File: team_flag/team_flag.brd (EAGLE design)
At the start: 40.6 x 40.6 mm, 11 parts, among them Q1 MOSFET-LOGIC-NCHANNELSMD, Q2 MOSFET-LOGIC-NCHANNELSMD

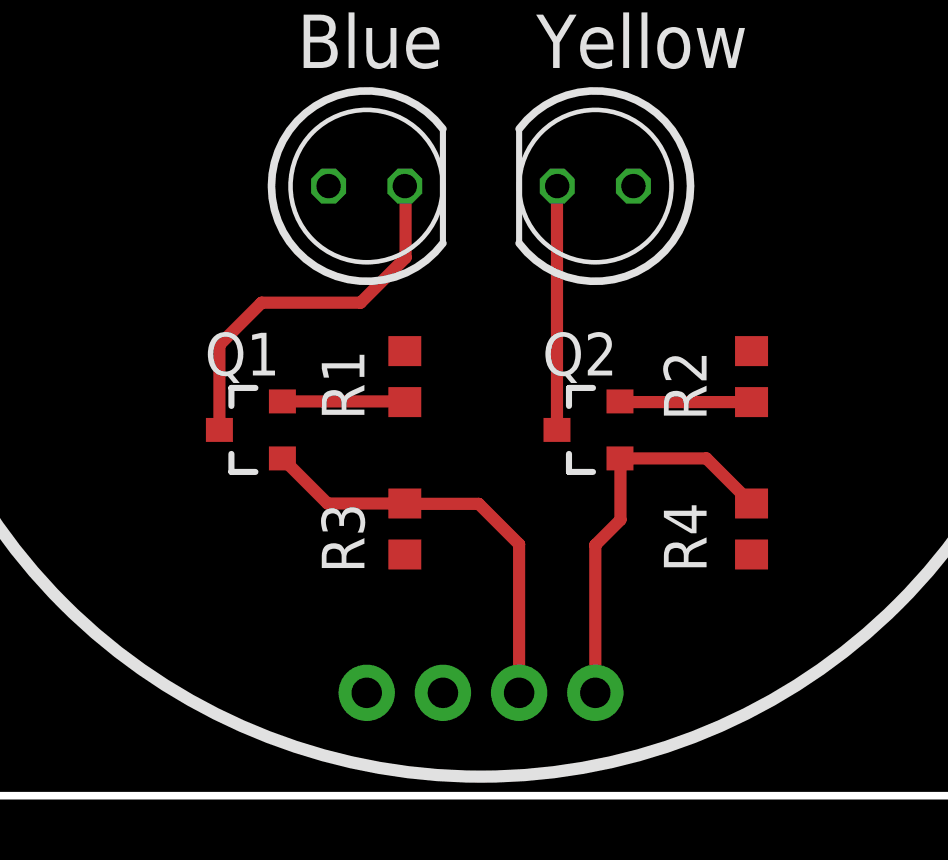
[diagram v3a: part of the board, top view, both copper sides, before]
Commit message: Team Flag Rev C pt 2
-changed resistors from 200 to 330
-moved 330 resistors to the drain-side of the MOSFETs
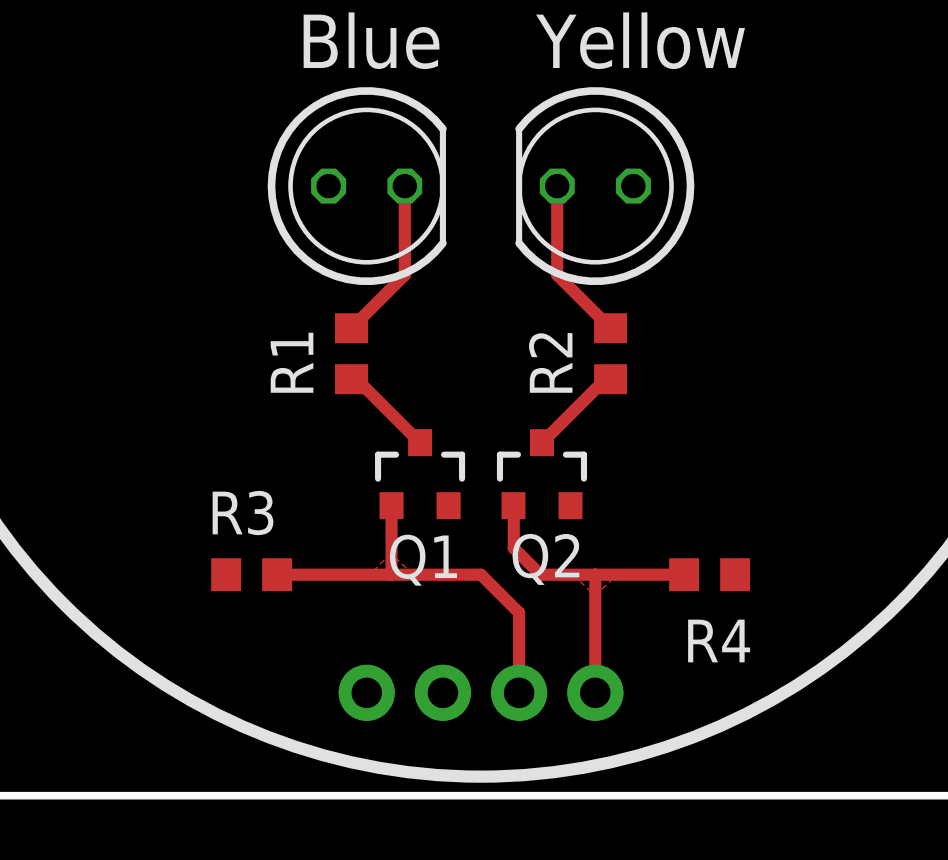
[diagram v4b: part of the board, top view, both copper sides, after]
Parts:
- R1, R2: value 200 -> 330
- moved Q1 5.79 mm to (18.3, 10.7), turned to 0 degrees
- moved R3 5.33 mm to (12.7, 7.37), turned to 0 degrees
- moved R2 4.76 mm to (24.6, 14.7), turned to 90 degrees
- moved Q2 2.21 mm to (22.4, 10.7), turned to 0 degrees
- moved R4 2.07 mm to (27.9, 7.37), turned to 180 degrees
- moved R1 1.93 mm to (16.0, 14.7), turned to 90 degrees
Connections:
- removed net BDRAIN: LED1.K, Q1.3
- removed net YDRAIN: LED2.K, Q2.3
- new net N$2: LED1.K, R1.2
- new net N$3: LED2.K, R2.2
- net BSOURCE: now also Q1.3, R1.1; no longer Q1.2, R1.2
- net GND: now also Q1.2, Q2.2; no longer R1.1, R2.1
- net YSOURCE: now also Q2.3, R2.1; no longer Q2.2, R2.2
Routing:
- net BDRAIN: track 12.6 -> 0.00 mm
- net YDRAIN: track 8.13 -> 0.00 mm
- net N$3: track 0.00 -> 5.47 mm
- net N$2: track 0.00 -> 5.47 mm
- net YELLOW: track 13.2 -> 11.4 mm
- net YSOURCE: track 4.41 -> 3.16 mm
- net BSOURCE: track 4.10 -> 3.16 mm
- added copper zone on layer 1, net BLUE
- added copper zone on layer 1, net YELLOW
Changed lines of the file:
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@@
 <attribute name="VALUE" x="20.9296" y="22.1234" size="1.27" layer="27" ratio="10" rot="R180"/>
 </element>
-<element name="R1" library="rcl" package="R0603" value="200" x="17.78" y="13.97" smashed="yes" rot="R270">
-<attribute name="NAME" x="16.4338" y="12.5222" size="1.4224" layer="25" font="vector" rot="R90"/>
-<attribute name="VALUE" x="20.5232" y="12.4968" size="1.4224" layer="27" font="vector" rot="R90"/>
+<element name="R1" library="rcl" package="R0603" value="330" x="16.002" y="14.732" smashed="yes" rot="R90">
+<attribute name="NAME" x="14.732" y="13.2588" size="1.4224" layer="25" font="vector" rot="R90"/>
+<attribute name="VALUE" x="17.272" y="13.2588" size="1.4224" layer="27" font="vector" rot="R270" align="bottom-right"/>
 </element>
-<element name="R2" library="rcl" package="R0603" value="200" x="29.337" y="13.97" smashed="yes" rot="R270">
-<attribute name="NAME" x="27.8384" y="12.4968" size="1.4224" layer="25" font="vector" rot="R90"/>
-<attribute name="VALUE" x="32.004" y="12.4968" size="1.4224" layer="27" font="vector" rot="R90"/>
+<element name="R2" library="rcl" package="R0603" value="330" x="24.638" y="14.732" smashed="yes" rot="R90">
+<attribute name="NAME" x="23.368" y="13.2588" size="1.4224" layer="25" font="vector" rot="R90"/>
+<attribute name="VALUE" x="25.8826" y="13.2588" size="1.4224" layer="27" font="vector" rot="R270" align="bottom-right"/>
 </element>
 <element name="U$2" library="pie" package="OSHW-LOGO-S" value="" x="20.32" y="31.75" rot="MR0"/>
 <element name="U$1" library="pie" package="PIE-LOGO-SMALL" value="" x="33.655" y="16.51" rot="MR0"/>
-<element name="Q1" library="pie" package="SOT23-3-LOGIC" value="MOSFET-LOGIC-NCHANNELSMD" x="12.7" y="12.192" smashed="yes" rot="R90">
-<attribute name="NAME" x="13.6144" y="15.4305" size="1.4224" layer="25" font="vector" align="top-right"/>
-<attribute name="PIE_DIGIKEY-PN" value="DMN65D8L-7DICT-ND" x="12.7" y="12.192" size="1.778" layer="27" rot="R90" display="off"/>
+<element name="Q1" library="pie" package="SOT23-3-LOGIC" value="MOSFET-LOGIC-NCHANNELSMD" x="18.288" y="10.668" smashed="yes">
+<attribute name="NAME" x="19.685" y="7.2517" size="1.4224" layer="25" font="vector" rot="R180" align="top-left"/>
+<attribute name="PIE_DIGIKEY-PN" value="DMN65D8L-7DICT-ND" x="18.288" y="10.668" size="1.778" layer="27" display="off"/>
 </element>
-<element name="Q2" library="pie" package="SOT23-3-LOGIC" value="MOSFET-LOGIC-NCHANNELSMD" x="23.9522" y="12.192" smashed="yes" rot="R90">
-<attribute name="NAME" x="24.8666" y="15.4305" size="1.4224" layer="25" font="vector" rot="R180"/>
-<attribute name="PIE_DIGIKEY-PN" value="DMN65D8L-7DICT-ND" x="23.9522" y="12.192" size="1.778" layer="27" rot="R90" display="off"/>
+<element name="Q2" library="pie" package="SOT23-3-LOGIC" value="MOSFET-LOGIC-NCHANNELSMD" x="22.352" y="10.668" smashed="yes">
+<attribute name="NAME" x="23.7744" y="7.2771" size="1.4224" layer="25" font="vector" align="bottom-right"/>
+<attribute name="PIE_DIGIKEY-PN" value="DMN65D8L-7DICT-ND" x="22.352" y="10.668" size="1.778" layer="27" display="off"/>
 </element>
-<element name="R3" library="rcl" package="R0603" value="10K" x="17.78" y="8.89" smashed="yes" rot="R90">
-<attribute name="NAME" x="16.4338" y="7.4168" size="1.4224" layer="25" font="vector" rot="R90"/>
-<attribute name="VALUE" x="20.5232" y="7.4168" size="1.4224" layer="27" font="vector" rot="R90"/>
+<element name="R3" library="rcl" package="R0603" value="10K" x="12.6746" y="7.366" smashed="yes">
+<attribute name="NAME" x="11.2014" y="8.7122" size="1.4224" layer="25" font="vector"/>
+<attribute name="VALUE" x="11.2014" y="4.6228" size="1.4224" layer="27" font="vector"/>
 </element>
-<element name="R4" library="rcl" package="R0603" value="10K" x="29.337" y="8.89" smashed="yes" rot="R90">
-<attribute name="NAME" x="27.8384" y="7.4422" size="1.4224" layer="25" font="vector" rot="R90"/>
-<attribute name="VALUE" x="32.1564" y="7.4168" size="1.4224" layer="27" font="vector" rot="R90"/>
+<element name="R4" library="rcl" package="R0603" value="10K" x="27.94" y="7.366" smashed="yes" rot="R180">
+<attribute name="NAME" x="29.3878" y="5.8674" size="1.4224" layer="25" font="vector" rot="R180"/>
+<attribute name="VALUE" x="29.4132" y="10.1854" size="1.4224" layer="27" font="vector" rot="R180"/>
 </element>
 <element name="JP1" library="pie" package="1X04-MTA" value="" x="20.32" y="3.429" smashed="yes" rot="MR180">
@@
 <contactref element="R4" pad="2"/>
 <contactref element="JP1" pad="4"/>
-<wire x1="24.13" y1="3.429" x2="24.13" y2="8.3566" width="0.4064" layer="1"/>
-<wire x1="24.13" y1="8.3566" x2="24.9682" y2="9.1948" width="0.4064" layer="1"/>
-<wire x1="24.9682" y1="9.1948" x2="24.9682" y2="11.226" width="0.4064" layer="1"/>
-<wire x1="24.9682" y1="11.226" x2="24.9522" y2="11.242" width="0.4064" layer="1"/>
-<wire x1="29.337" y1="9.74" x2="27.835" y2="11.242" width="0.4064" layer="1"/>
-<wire x1="27.835" y1="11.242" x2="24.9522" y2="11.242" width="0.4064" layer="1"/>
+<wire x1="27.09" y1="7.366" x2="24.13" y2="7.366" width="0.4064" layer="1"/>
+<wire x1="24.13" y1="7.366" x2="22.3012" y2="7.366" width="0.4064" layer="1"/>
+<wire x1="22.3012" y1="7.366" x2="21.4122" y2="8.255" width="0.4064" layer="1"/>
+<wire x1="21.4122" y1="8.255" x2="21.4122" y2="9.6578" width="0.4064" layer="1"/>
+<wire x1="21.4122" y1="9.6578" x2="21.402" y2="9.668" width="0.4064" layer="1"/>
+<wire x1="24.13" y1="3.429" x2="24.13" y2="7.366" width="0.4064" layer="1"/>
+<polygon width="0.4064" layer="1" spacing="0.6096">
+<vertex x="23.3934" y="7.366"/>
+<vertex x="24.13" y="6.6548"/>
+<vertex x="24.8412" y="7.366"/>
+</polygon>
 </signal>
 <signal name="VCC">
@@
 </signal>
 <signal name="GND">
-<contactref element="R1" pad="1"/>
-<contactref element="R2" pad="1"/>
 <polygon width="0.4064" layer="1" rank="2">
 <vertex x="0" y="0"/>
@@
 <contactref element="R4" pad="1"/>
 <contactref element="JP1" pad="1"/>
+<contactref element="Q1" pad="2"/>
+<contactref element="Q2" pad="2"/>
 </signal>
 <signal name="BLUE">
@@
 <contactref element="R3" pad="2"/>
 <contactref element="JP1" pad="3"/>
-<wire x1="21.59" y1="3.429" x2="21.59" y2="8.382" width="0.4064" layer="1"/>
-<wire x1="21.59" y1="8.382" x2="20.2438" y2="9.7282" width="0.4064" layer="1"/>
-<wire x1="20.2438" y1="9.7282" x2="17.7918" y2="9.7282" width="0.4064" layer="1"/>
-<wire x1="17.7918" y1="9.7282" x2="17.78" y2="9.74" width="0.4064" layer="1"/>
-<wire x1="17.78" y1="9.74" x2="15.202" y2="9.74" width="0.4064" layer="1"/>
-<wire x1="15.202" y1="9.74" x2="13.7" y2="11.242" width="0.4064" layer="1"/>
-</signal>
-<signal name="BDRAIN">
-<contactref element="LED1" pad="K"/>
-<contactref element="Q1" pad="3"/>
-<wire x1="11.6" y1="12.192" x2="11.6" y2="15.029" width="0.4064" layer="1"/>
-<wire x1="11.6" y1="15.029" x2="13.0048" y2="16.4338" width="0.4064" layer="1"/>
-<wire x1="13.0048" y1="16.4338" x2="16.3068" y2="16.4338" width="0.4064" layer="1"/>
-<wire x1="16.3068" y1="16.4338" x2="17.8054" y2="17.9324" width="0.4064" layer="1"/>
-<wire x1="17.8054" y1="17.9324" x2="17.8054" y2="20.2946" width="0.4064" layer="1"/>
-<wire x1="17.8054" y1="20.2946" x2="17.78" y2="20.32" width="0.4064" layer="1"/>
+<wire x1="21.59" y1="3.429" x2="21.59" y2="6.096" width="0.4064" layer="1"/>
+<wire x1="21.59" y1="6.096" x2="20.32" y2="7.366" width="0.4064" layer="1"/>
+<wire x1="20.32" y1="7.366" x2="17.2974" y2="7.366" width="0.4064" layer="1"/>
+<wire x1="17.2974" y1="7.366" x2="13.5246" y2="7.366" width="0.4064" layer="1"/>
+<wire x1="17.338" y1="9.668" x2="17.338" y2="7.4066" width="0.4064" layer="1"/>
+<wire x1="17.338" y1="7.4066" x2="17.2974" y2="7.366" width="0.4064" layer="1"/>
+<polygon width="0.4064" layer="1" spacing="0.6096">
+<vertex x="18.0594" y="7.366"/>
+<vertex x="17.3228" y="8.0772"/>
+<vertex x="16.6116" y="7.366"/>
+</polygon>
 </signal>
 <signal name="BSOURCE">
-<contactref element="Q1" pad="2"/>
+<contactref element="Q1" pad="3"/>
+<contactref element="R1" pad="1"/>
+<wire x1="16.002" y1="13.882" x2="16.174" y2="13.882" width="0.4064" layer="1"/>
+<wire x1="16.174" y1="13.882" x2="18.288" y2="11.768" width="0.4064" layer="1"/>
+</signal>
+<signal name="N$2">
 <contactref element="R1" pad="2"/>
-<wire x1="13.7" y1="13.142" x2="17.78" y2="13.142" width="0.4064" layer="1"/>
-<wire x1="17.78" y1="13.142" x2="17.78" y2="13.12" width="0.4064" layer="1"/>
+<contactref element="LED1" pad="K"/>
+<wire x1="16.002" y1="15.582" x2="17.78" y2="17.36" width="0.4064" layer="1"/>
+<wire x1="17.78" y1="17.36" x2="17.78" y2="20.32" width="0.4064" layer="1"/>
 </signal>
-<signal name="YDRAIN">
+<signal name="N$3">
 <contactref element="LED2" pad="K"/>
-<contactref element="Q2" pad="3"/>
-<wire x1="22.8522" y1="12.192" x2="22.8522" y2="20.3122" width="0.4064" layer="1"/>
-<wire x1="22.8522" y1="20.3122" x2="22.86" y2="20.32" width="0.4064" layer="1"/>
+<contactref element="R2" pad="2"/>
+<wire x1="24.638" y1="15.582" x2="22.86" y2="17.36" width="0.4064" layer="1"/>
+<wire x1="22.86" y1="17.36" x2="22.86" y2="20.32" width="0.4064" layer="1"/>
 </signal>
 <signal name="YSOURCE">
-<contactref element="Q2" pad="2"/>
-<contactref element="R2" pad="2"/>
-<wire x1="29.337" y1="13.12" x2="24.9522" y2="13.12" width="0.4064" layer="1"/>
-<wire x1="24.9522" y1="13.12" x2="24.9522" y2="13.142" width="0.4064" layer="1"/>
+<contactref element="R2" pad="1"/>
+<contactref element="Q2" pad="3"/>
+<wire x1="24.638" y1="13.882" x2="24.466" y2="13.882" width="0.4064" layer="1"/>
+<wire x1="24.466" y1="13.882" x2="22.352" y2="11.768" width="0.4064" layer="1"/>
 </signal>
 </signals>

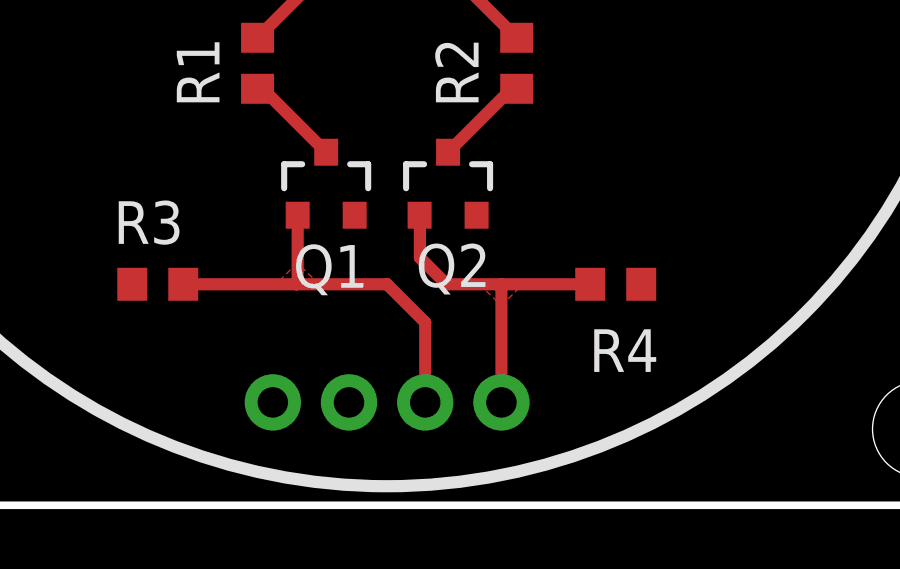
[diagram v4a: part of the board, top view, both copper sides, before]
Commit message: Team Flag Rev C pt 3
-reoriented MTA connector footprint
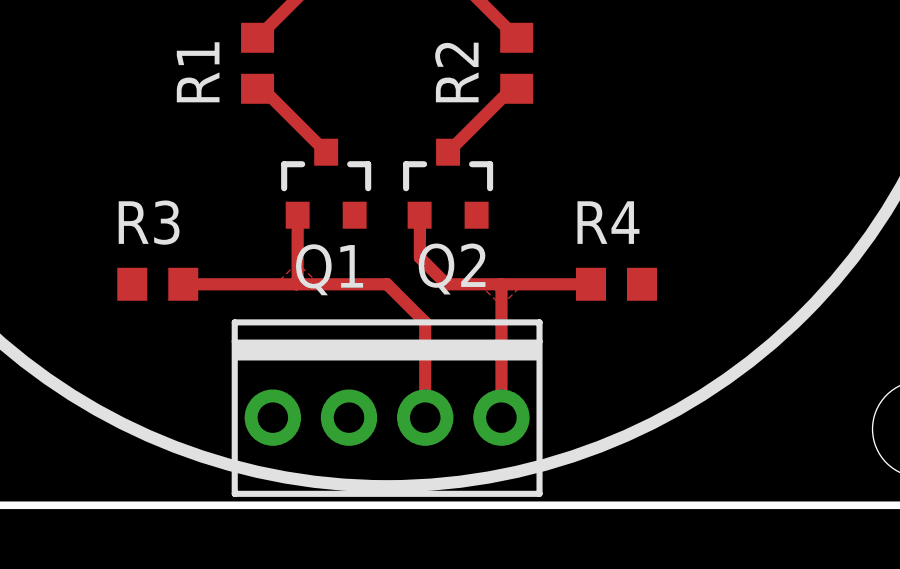
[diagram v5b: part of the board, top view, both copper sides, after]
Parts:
- moved JP1 0.51 mm to (20.3, 2.92), flipped to the top, turned to 0 degrees
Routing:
- net YELLOW: track 11.4 -> 11.9 mm
- net BLUE: track 13.6 -> 14.1 mm
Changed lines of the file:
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@@
 <attribute name="VALUE" x="11.2014" y="4.6228" size="1.4224" layer="27" font="vector"/>
 </element>
-<element name="R4" library="rcl" package="R0603" value="10K" x="27.94" y="7.366" smashed="yes" rot="R180">
-<attribute name="NAME" x="29.3878" y="5.8674" size="1.4224" layer="25" font="vector" rot="R180"/>
-<attribute name="VALUE" x="29.4132" y="10.1854" size="1.4224" layer="27" font="vector" rot="R180"/>
+<element name="R4" library="rcl" package="R0603" value="10K" x="27.9654" y="7.366" smashed="yes" rot="R180">
+<attribute name="NAME" x="26.4922" y="8.7122" size="1.4224" layer="25" font="vector" rot="R180" align="top-right"/>
+<attribute name="VALUE" x="26.4922" y="4.6228" size="1.4224" layer="27" font="vector" rot="R180" align="top-right"/>
 </element>
-<element name="JP1" library="pie" package="1X04-MTA" value="" x="20.32" y="3.429" smashed="yes" rot="MR180">
-<attribute name="PARTNUMBER" value="A1922-ND" x="20.32" y="3.429" size="1.778" layer="28" rot="MR180" display="off"/>
-<attribute name="VALUE" x="15.875" y="7.874" size="1.27" layer="28" font="vector" rot="MR180"/>
+<element name="JP1" library="pie" package="1X04-MTA" value="" x="20.32" y="2.921" smashed="yes">
+<attribute name="PARTNUMBER" value="A1922-ND" x="20.32" y="2.921" size="1.778" layer="27" display="off"/>
+<attribute name="VALUE" x="15.875" y="-1.524" size="1.27" layer="27" font="vector"/>
 </element>
 </elements>
@@
 <contactref element="R4" pad="2"/>
 <contactref element="JP1" pad="4"/>
-<wire x1="27.09" y1="7.366" x2="24.13" y2="7.366" width="0.4064" layer="1"/>
-<wire x1="24.13" y1="7.366" x2="22.3012" y2="7.366" width="0.4064" layer="1"/>
+<wire x1="27.1154" y1="7.366" x2="24.1046" y2="7.366" width="0.4064" layer="1"/>
+<wire x1="24.1046" y1="7.366" x2="22.3012" y2="7.366" width="0.4064" layer="1"/>
 <wire x1="22.3012" y1="7.366" x2="21.4122" y2="8.255" width="0.4064" layer="1"/>
 <wire x1="21.4122" y1="8.255" x2="21.4122" y2="9.6578" width="0.4064" layer="1"/>
 <wire x1="21.4122" y1="9.6578" x2="21.402" y2="9.668" width="0.4064" layer="1"/>
-<wire x1="24.13" y1="3.429" x2="24.13" y2="7.366" width="0.4064" layer="1"/>
 <polygon width="0.4064" layer="1" spacing="0.6096">
 <vertex x="23.3934" y="7.366"/>
@@
 <vertex x="24.8412" y="7.366"/>
 </polygon>
+<wire x1="24.13" y1="2.921" x2="24.13" y2="7.3406" width="0.4064" layer="1"/>
+<wire x1="24.13" y1="7.3406" x2="24.1046" y2="7.366" width="0.4064" layer="1"/>
 </signal>
 <signal name="VCC">
@@
 <contactref element="R3" pad="2"/>
 <contactref element="JP1" pad="3"/>
-<wire x1="21.59" y1="3.429" x2="21.59" y2="6.096" width="0.4064" layer="1"/>
 <wire x1="21.59" y1="6.096" x2="20.32" y2="7.366" width="0.4064" layer="1"/>
 <wire x1="20.32" y1="7.366" x2="17.2974" y2="7.366" width="0.4064" layer="1"/>
@@
 <vertex x="16.6116" y="7.366"/>
 </polygon>
+<wire x1="21.59" y1="2.921" x2="21.59" y2="6.096" width="0.4064" layer="1"/>
 </signal>
 <signal name="BSOURCE">

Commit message: Team Flag Rev C pt 4
-reoriented MTA footprint again
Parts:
- flipped JP1 to the bottom
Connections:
- net BLUE: now also JP1.2; no longer JP1.3
- net GND: now also JP1.4; no longer JP1.1
- net VCC: now also JP1.3; no longer JP1.2
- net YELLOW: now also JP1.1; no longer JP1.4
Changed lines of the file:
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@@
 <attribute name="VALUE" x="26.4922" y="4.6228" size="1.4224" layer="27" font="vector" rot="R180" align="top-right"/>
 </element>
-<element name="JP1" library="pie" package="1X04-MTA" value="" x="20.32" y="2.921" smashed="yes">
-<attribute name="PARTNUMBER" value="A1922-ND" x="20.32" y="2.921" size="1.778" layer="27" display="off"/>
-<attribute name="VALUE" x="15.875" y="-1.524" size="1.27" layer="27" font="vector"/>
+<element name="JP1" library="pie" package="1X04-MTA" value="" x="20.32" y="2.921" smashed="yes" rot="MR0">
+<attribute name="PARTNUMBER" value="A1922-ND" x="20.32" y="2.921" size="1.778" layer="28" rot="MR0" display="off"/>
+<attribute name="VALUE" x="24.765" y="-1.524" size="1.27" layer="28" font="vector" rot="MR0"/>
 </element>
 </elements>
@@
 <contactref element="Q2" pad="1"/>
 <contactref element="R4" pad="2"/>
-<contactref element="JP1" pad="4"/>
 <wire x1="27.1154" y1="7.366" x2="24.1046" y2="7.366" width="0.4064" layer="1"/>
 <wire x1="24.1046" y1="7.366" x2="22.3012" y2="7.366" width="0.4064" layer="1"/>
@@
 <vertex x="24.8412" y="7.366"/>
 </polygon>
+<wire x1="24.13" y1="7.3406" x2="24.1046" y2="7.366" width="0.4064" layer="1"/>
+<contactref element="JP1" pad="1"/>
 <wire x1="24.13" y1="2.921" x2="24.13" y2="7.3406" width="0.4064" layer="1"/>
-<wire x1="24.13" y1="7.3406" x2="24.1046" y2="7.366" width="0.4064" layer="1"/>
 </signal>
 <signal name="VCC">
@@
 <contactref element="LED1" pad="A"/>
 <contactref element="LED2" pad="A"/>
-<contactref element="JP1" pad="2"/>
+<contactref element="JP1" pad="3"/>
 </signal>
 <signal name="GND">
@@
 <contactref element="R3" pad="1"/>
 <contactref element="R4" pad="1"/>
-<contactref element="JP1" pad="1"/>
 <contactref element="Q1" pad="2"/>
 <contactref element="Q2" pad="2"/>
+<contactref element="JP1" pad="4"/>
 </signal>
 <signal name="BLUE">
 <contactref element="Q1" pad="1"/>
 <contactref element="R3" pad="2"/>
-<contactref element="JP1" pad="3"/>
 <wire x1="21.59" y1="6.096" x2="20.32" y2="7.366" width="0.4064" layer="1"/>
 <wire x1="20.32" y1="7.366" x2="17.2974" y2="7.366" width="0.4064" layer="1"/>
@@
 <vertex x="16.6116" y="7.366"/>
 </polygon>
-<wire x1="21.59" y1="2.921" x2="21.59" y2="6.096" width="0.4064" layer="1"/>
+<contactref element="JP1" pad="2"/>
+<wire x1="21.59" y1="6.096" x2="21.59" y2="2.921" width="0.4064" layer="1"/>
 </signal>
 <signal name="BSOURCE">
